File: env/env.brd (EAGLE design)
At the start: 81.3 x 107.6 mm, 73 parts, among them IC1 DG403DJD, IC2 OPA4130U, IC3 4001D, IC4 OPA2134D, IC5 OPA4130U, Q1 BC847ALT1SMD, Q2 BC857ALT1SMD, X1 2516-

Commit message: more work on the env.
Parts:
- added C10, C11, C12, C13, C14, C5, C6, C7, C8, C9: 1u, dan:C0603
- moved C3 5.24 mm to (22.9, 55.9)
- moved EOF 4.02 mm to (58.4, 25.4)
- moved EOR 4.02 mm to (29.2, 25.4)
- moved R14 4.02 mm to (38.1, 22.9)
- moved R15 4.02 mm to (40.6, 22.9)
- moved R24 4.02 mm to (44.5, 21.6)
- moved R33 3.81 mm to (66.0, 47.0)
- moved R34 3.81 mm to (66.0, 44.5)
- moved R35 3.81 mm to (66.0, 53.3)
- moved ACV 3.81 mm to (29.2, 10.2)
- moved ADAR 3.81 mm to (52.1, 88.9)
- moved AUV 3.81 mm to (43.2, 45.7)
- moved C4 3.81 mm to (29.2, 83.8)
- moved CVOUT 3.81 mm to (74.9, 10.2)
- moved D 3.81 mm to (72.4, 92.7)
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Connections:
- net +12V: now also C5.1, C6.1, C7.1, C8.1, C9.1
- net -12V: now also C10.1, C11.1, C12.1, C13.1, C14.1
- net GND: now also C10.2, C11.2, C12.2, C13.2, C14.2, C5.2, C6.2, C7.2, C8.2, C9.2
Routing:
- net N$9: track 71.1 -> 176.7 mm, vias 5 -> 8
- net N$7: track 0.00 -> 103.6 mm, vias 0 -> 4
- net +12V: track 279.0 -> 378.3 mm, vias 18 -> 22
- net N$3: track 2.54 -> 56.3 mm, vias 0 -> 2
- net ENV: track 145.2 -> 177.8 mm, vias 8 -> 10
- net -12V: track 313.0 -> 330.9 mm, vias 14 -> 15
- net N$48: track 45.6 -> 55.7 mm
- net N$38: track 72.7 -> 69.0 mm
- net N$21: track 11.8 -> 14.7 mm
- net N$16: track 61.9 -> 64.7 mm
- net N$36: track 69.1 -> 71.6 mm
- net N$28: track 4.77 -> 2.33 mm
- net N$30: track 4.77 -> 2.33 mm
- net N$25: track 4.77 -> 2.33 mm
- net N$29: track 4.77 -> 2.33 mm
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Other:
- board size 81.3 x 107.6 mm -> 86.3 x 107.6 mm

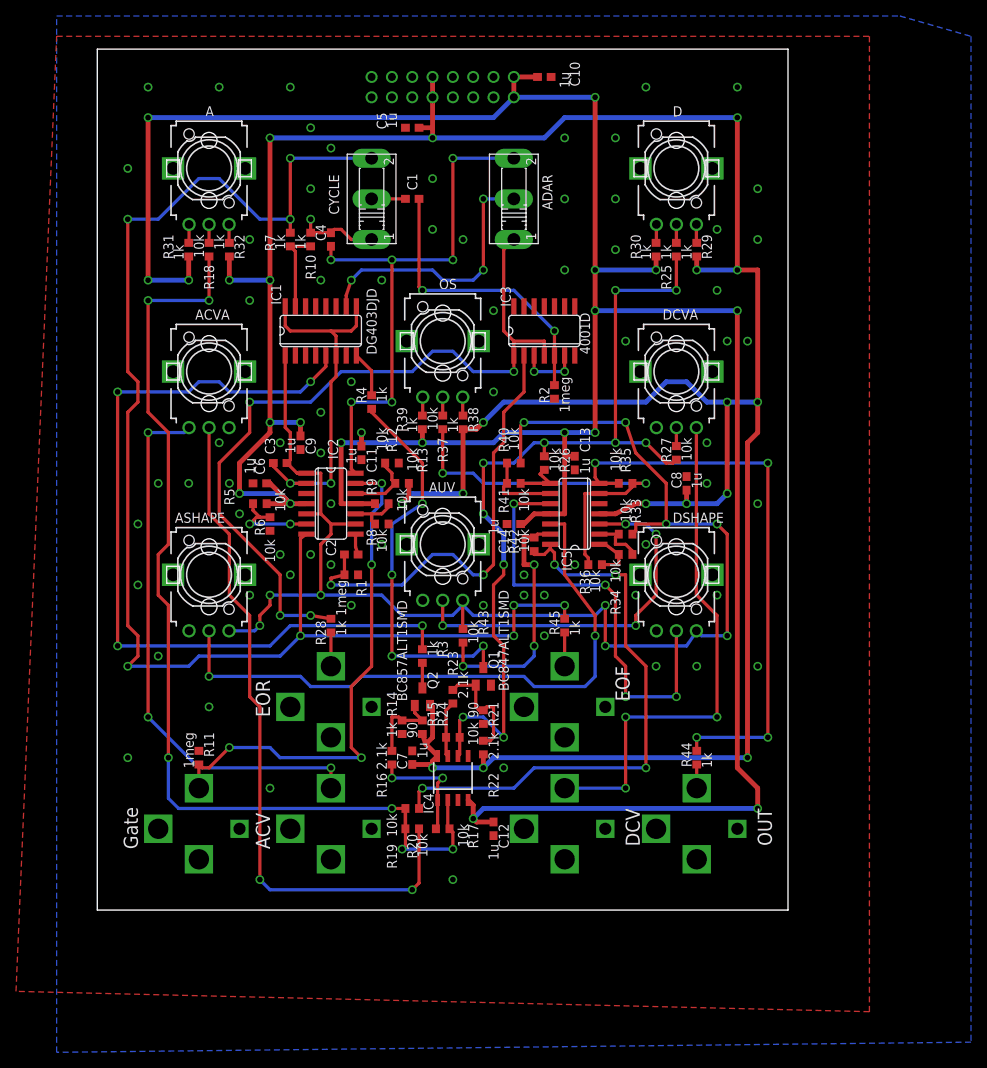
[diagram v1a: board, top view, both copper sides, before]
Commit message: almost done with the env.  need to check things (pot polarity)
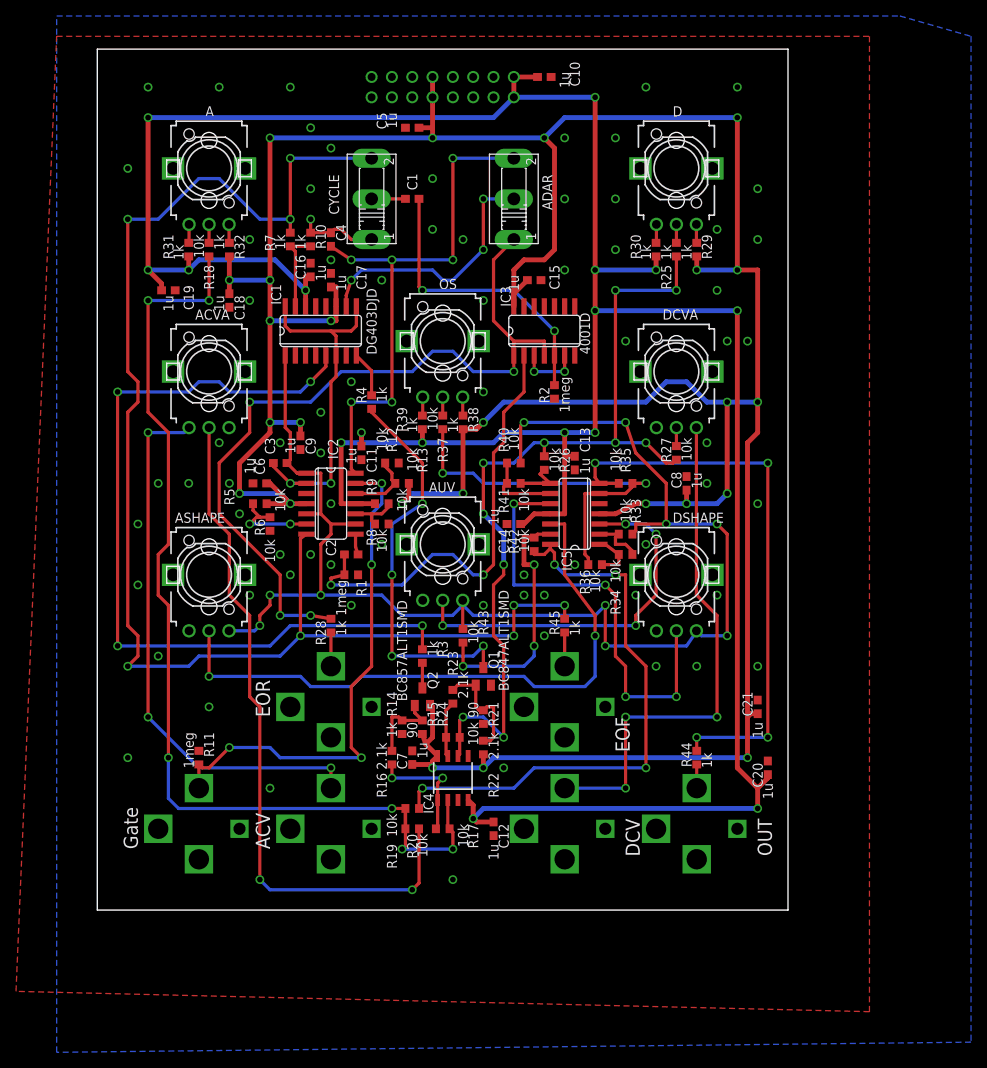
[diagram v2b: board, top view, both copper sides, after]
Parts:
- added C15, C16, C17, C18, C19, C20, C21: 1u, dan:C0603
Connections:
- removed net V+: IC1.11
- removed net V-: IC1.14
- removed net VDD: IC3.14
- removed net VSS: IC3.7
- net +12V: now also C15.1, C17.1, C18.1, C21.1, IC1.11, IC3.14
- net -12V: now also C16.1, C19.1, C20.1, IC1.14
- net GND: now also C15.2, C16.2, C17.2, C18.2, C19.2, C20.2, C21.2, IC3.7
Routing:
- net +12V: track 378.3 -> 423.7 mm, vias 22 -> 25
- net -12V: track 330.9 -> 354.8 mm, vias 15 -> 16
- net N$18: track 34.2 -> 32.7 mm
- net N$20: track 69.2 -> 68.0 mm
- net N$2: track 97.7 -> 98.7 mm

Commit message: added leds to env
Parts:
- added D1: (no value), dan:DUOLED5MM
- added LED1, LED2: (no value), dan:LED5MM
- added R46, R47, R48: 10k, dan:R0603
- moved C1 2.54 mm to (39.4, 86.4), turned to 90 degrees
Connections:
- new net N$43: LED2.K, R46.2
- new net N$52: D1.AG, D1.AR, R48.1
- new net N$53: LED1.K, R47.2
- net GND: now also R46.1, R47.1, R48.2
- net N$2: now also LED2.A
- net N$36: now also D1.K
- net N$9: now also LED1.A
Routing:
- net N$36: track 71.6 -> 147.7 mm, vias 4 -> 5
- net N$9: track 176.7 -> 214.1 mm, vias 8 -> 10
- net N$2: track 98.7 -> 117.6 mm, vias 4 -> 5
- net N$52: track 0.00 -> 11.6 mm
- net N$48: track 55.7 -> 48.9 mm
- net N$43: track 0.00 -> 5.25 mm
- net N$44: track 65.2 -> 69.5 mm
- net N$53: track 0.00 -> 2.96 mm
- net N$19: track 4.23 -> 6.03 mm
- net +12V: track 423.7 -> 422.2 mm
- net N$18: track 32.7 -> 33.8 mm
- net N$50: track 86.7 -> 87.7 mm
